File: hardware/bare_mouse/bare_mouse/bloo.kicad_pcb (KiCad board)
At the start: 2 copper layers, 103 parts, among them J1 Serial Debug Header, J10 Conn_01x06_Female, J2 SWD Header, J4 Conn_ARM_JTAG_SWD_10, J5 SWD Header, M1 M1_Conn_Alt, M2 M2_Conn_Alt, Q0 TEFT4300, Q1 TEFT4300, Q10 Q_NMOS_GSD, Q11 Q_NMOS_GSD, Q12 Q_NMOS_GSD, Q2 TEFT4300, Q3 TEFT4300, Q8 Q_NMOS_SGD, Q9 Q_NMOS_GSD, SW1 SW, SW2 SW, SW3 SW, U1 YAAJ_BluePill_SWD_Breakout, U2 L293D, U3 LM1085-5.0, U4 APE8865Y5-33-HF-3, U5 LM66100DCKR, U6 LM66100DCKR

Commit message: initial commit, starting adams pcb
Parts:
- C10: value 10uF(Tantalum) -> 10uF
- GND TP 2: renamed from TP2
- GND TP 5: renamed from TP5
- GND TP 6: renamed from TP6
- moved C1 213.4 mm to (390.6, 216.5), turned to 180 degrees
- moved C13 211.6 mm to (389.2, 225.8), turned to 180 degrees
- moved C9 210.3 mm to (392.2, 219.5), turned to 180 degrees
- moved C10 209.9 mm to (391.9, 222.5), turned to 180 degrees
- moved U3 207.7 mm to (371.1, 217.5), turned to 90 degrees
- moved BZ1 203.5 mm to (36.9, 3.28)
- moved J4 188.6 mm to (379.4, 174.7)
- moved R4 180.8 mm to (381.6, 149.9)
- moved U6 179.9 mm to (72.9, 120.1)
- moved M_MH1 179.1 mm to (342.9, 198.5)
- moved S1 178.7 mm to (349.8, 221.7)
- moved R3 175.0 mm to (375.6, 143.0)
- moved D3 170.1 mm to (384.6, 161.7), turned to 90 degrees
- moved R8 169.2 mm to (376.1, 145.9)
- moved R16 169.0 mm to (381.6, 145.9)
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- renumbered TP4 to 3V, TP3 to 5v, JP2 to JP_GND, JP3 to JP_RST, JP1 to JP_SWO, TP1 to V_EXT_TP
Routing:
- added copper zone on B.Cu, net GND
- added copper zone on F.Cu, net GND
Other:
- board outline added: 100.3 x 99 mm

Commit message: same as previous
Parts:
- C1, C10, C11, C12, C13, C14, C15, C17, C18, C19, C20, C21, C25, C3, C4, C9, L1, Q8, R11, R12, R17, R18, R19, R20, R21, R22, R23, R24, R9, U4: moved to B.Cu
- moved BZ1 364.0 mm to (327.8, 222.1), turned to 180 degrees
- moved J10 290.5 mm to (369.8, 168.2)
- moved C19 290.1 mm to (317.7, 217.9), turned to -90 degrees
- moved FB3 279.0 mm to (364.5, 187.7), turned to 180 degrees
- moved C6 277.7 mm to (359.1, 187.7), turned to 180 degrees
- moved BT_MH3 277.3 mm to (367.6, 149.2)
- moved BT_MH4 277.3 mm to (367.6, 155.2)
- moved BT_MH1 277.3 mm to (361.6, 149.2)
- moved BT_MH2 277.3 mm to (361.6, 155.2)
- moved FB4 276.5 mm to (364.5, 186.0), turned to 180 degrees
- moved C8 275.1 mm to (359.1, 186.0), turned to 180 degrees
- moved RST1 262.8 mm to (315.8, 221.1), turned to 90 degrees
- moved SW1 262.5 mm to (300.6, 221.1), turned to 90 degrees
- moved SW3 262.5 mm to (310.8, 221.1), turned to 90 degrees
- moved SW2 262.4 mm to (305.7, 221.1), turned to 90 degrees
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- renumbered SW_RST1 to RST1
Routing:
- net +3V3: track 0.00 -> 80.1 mm
- net BATT_NET: track 0.00 -> 63.5 mm, vias 0 -> 1
- net +5V_NET: track 0.00 -> 28.9 mm
- net +5V: track 0.00 -> 20.1 mm
- net Net-(S1-Pad3): track 0.00 -> 12.0 mm
- net 3V3_BYP: track 0.00 -> 7.52 mm
- net Net-(BT1-+): track 0.00 -> 6.09 mm
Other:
- board text added: "Muad' Dib Desert Mice"

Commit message: checkin changes
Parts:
- moved SK2 7.95 mm to (340.4, 131.7), turned to 180 degrees
- moved SK1 7.80 mm to (348.3, 131.7), turned to 180 degrees
- moved U1 2.68 mm to (345.2, 164.3), turned to 180 degrees

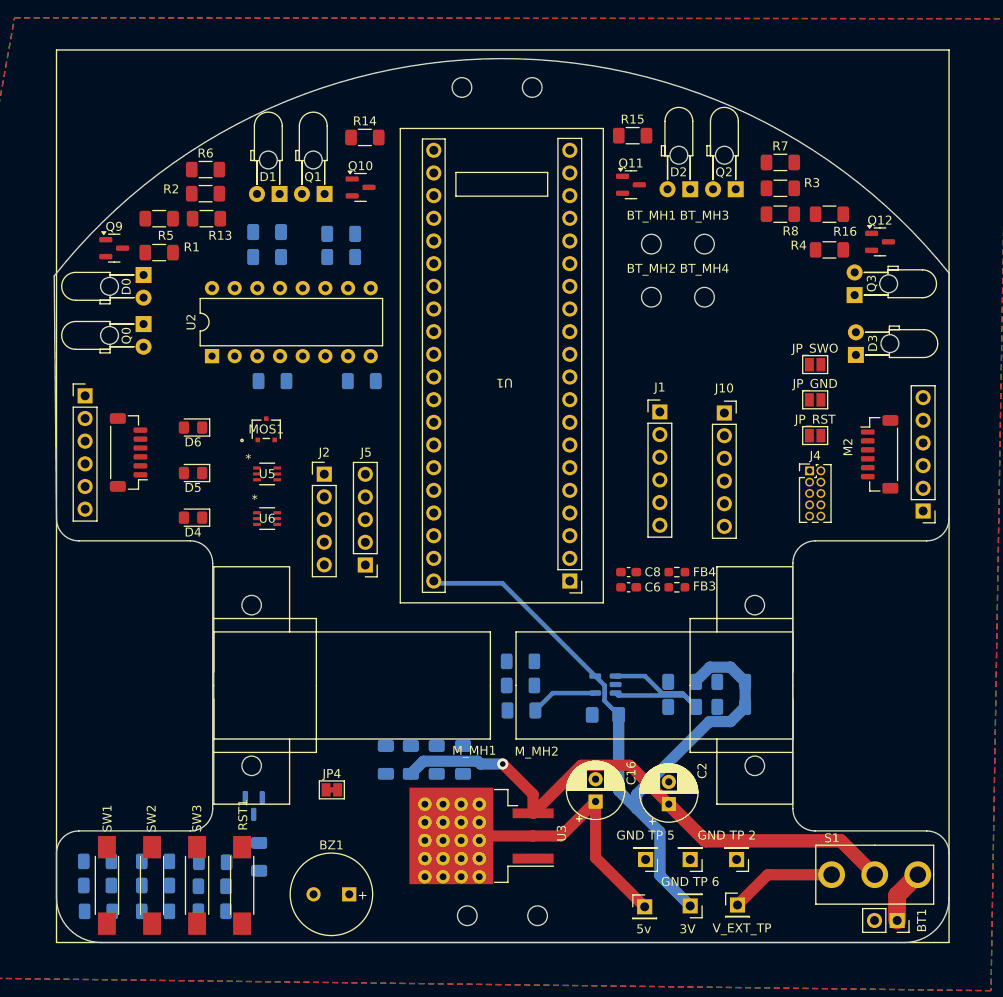
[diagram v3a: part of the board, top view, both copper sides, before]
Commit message: LED & switch wiring, mouse lost weight
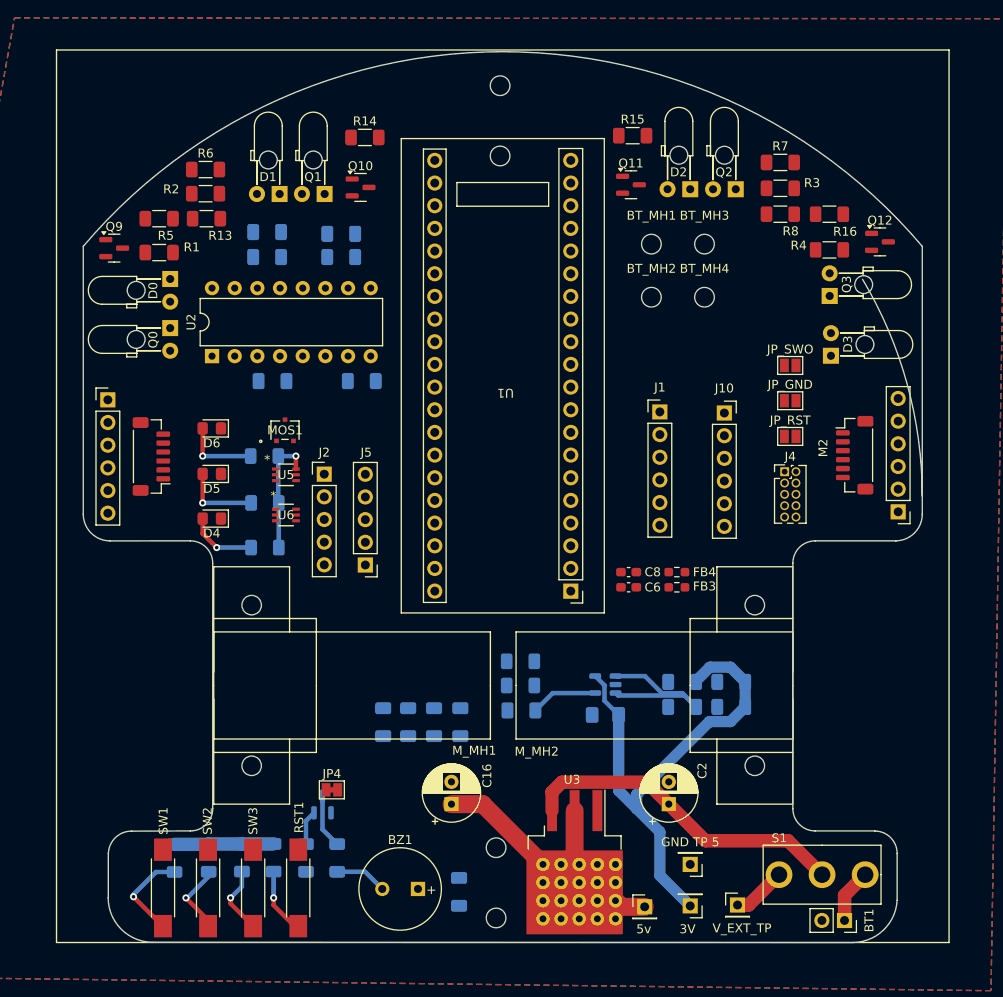
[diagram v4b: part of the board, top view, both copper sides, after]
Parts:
- removed GND TP 2: GND_TP, Connector_PinHeader_2.54mm:PinHeader_1x01_P2.54mm_Vertical
- removed GND TP 6: GND_TP, Connector_PinHeader_2.54mm:PinHeader_1x01_P2.54mm_Vertical
- moved R21 48.6 mm to (318.3, 173.0)
- moved R20 46.1 mm to (318.4, 178.2)
- moved R19 42.6 mm to (318.4, 183.2)
- moved C19 22.7 mm to (340.1, 221.8), turned to 90 degrees
- moved R18 20.4 mm to (326.4, 218.0), turned to -90 degrees
- moved R12 19.7 mm to (319.3, 218.0), turned to -90 degrees
- moved R9 17.2 mm to (315.8, 218.0), turned to -90 degrees
- moved R17 17.1 mm to (322.9, 218.0), turned to 90 degrees
- moved C16 16.2 mm to (339.2, 212.0)
- moved U3 11.3 mm to (345.0, 218.5), turned to -90 degrees
- moved R11 9.15 mm to (308.2, 218.1), turned to -90 degrees
- moved SK4 8.93 mm to (344.2, 216.9), turned to 90 degrees
- moved SK2 8.78 mm to (344.7, 139.4), turned to -90 degrees
- moved BZ1 7.72 mm to (335.5, 221.5)
- moved Q8 7.70 mm to (324.8, 212.0), turned to 90 degrees
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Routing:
- net BATT_NET: track 63.5 -> 37.1 mm, vias 1 -> 0
- net BUTTON: track 0.00 -> 10.6 mm, vias 0 -> 1
- net Net-(D5-A): track 0.00 -> 8.68 mm, vias 0 -> 1
- net Net-(D6-A): track 0.00 -> 8.47 mm, vias 0 -> 1
- net BUTTON_2: track 0.00 -> 8.26 mm, vias 0 -> 1
- net Net-(D4-A): track 0.00 -> 7.75 mm, vias 0 -> 1
- net BUTTON_3: track 0.00 -> 7.69 mm, vias 0 -> 1
- net RST: track 0.00 -> 7.50 mm, vias 0 -> 1
- net Net-(Q8-D): track 0.00 -> 6.06 mm
- net Net-(S1-Pad3): track 12.0 -> 6.06 mm
- net Net-(BZ1-+): track 0.00 -> 5.85 mm
- net BUZZER: track 0.00 -> 3.87 mm
- net +3V3: track 80.1 -> 82.5 mm, vias 0 -> 1
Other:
- board size 100.3 x 99 mm -> 94 x 99.8 mm

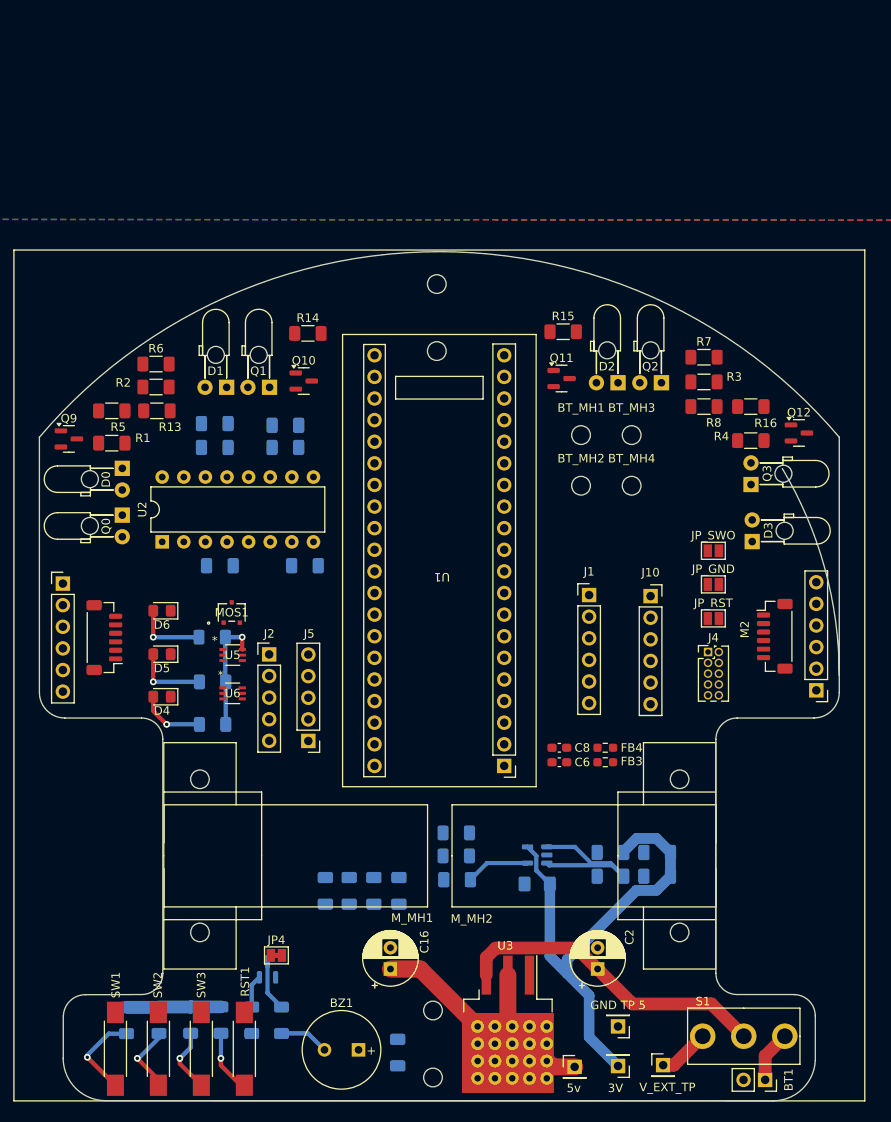
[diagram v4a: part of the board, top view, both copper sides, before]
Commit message: power ORing, SWD header, and other adam sections traced
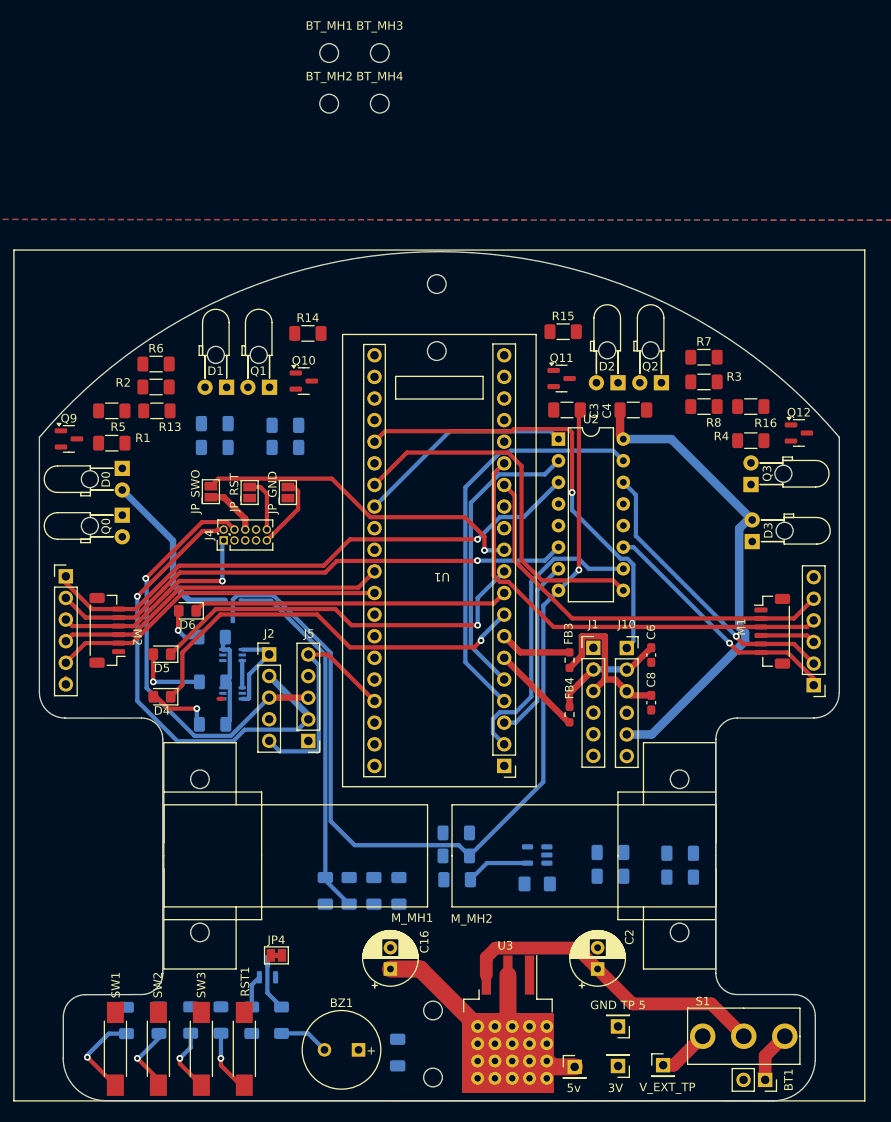
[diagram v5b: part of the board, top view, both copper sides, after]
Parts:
- C3, C4: moved to F.Cu
- MOS1, U5, U6: moved to B.Cu
- moved M1 94.8 mm to (392.2, 171.7), turned to 90 degrees
- moved M2 94.7 mm to (297.9, 172.8), turned to -90 degrees
- moved JP_SWO 59.5 mm to (318.1, 155.9), turned to 90 degrees
- moved J4 58.4 mm to (319.6, 161.6), turned to 90 degrees
- moved JP_RST 56.5 mm to (322.7, 156.0), turned to 90 degrees
- moved BT_MH3 53.8 mm to (338.0, 104.3)
- moved BT_MH4 53.8 mm to (338.0, 110.3)
- moved BT_MH1 53.8 mm to (332.1, 104.3)
- moved BT_MH2 53.8 mm to (332.1, 110.3)
- moved C4 51.9 mm to (367.8, 146.3), turned to 0 degrees
- moved JP_GND 51.2 mm to (327.2, 156.0), turned to 90 degrees
- moved U2 48.1 mm to (359.0, 149.7), turned to 0 degrees
- moved C3 35.8 mm to (360.0, 146.3), turned to 180 degrees
- moved C6 16.6 mm to (369.9, 175.1), turned to -90 degrees
- moved FB3 12.7 mm to (360.3, 175.7), turned to -90 degrees
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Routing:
- net VCC: track 0.00 -> 112.6 mm, vias 0 -> 1
- net M1_OUT_1: track 0.00 -> 66.1 mm, vias 0 -> 1
- net M1_OUT_2: track 0.00 -> 62.8 mm, vias 0 -> 1
- net +5V: track 20.1 -> 77.0 mm
- net SWDIO: track 0.00 -> 55.8 mm, vias 0 -> 1
- net M2_ENC_A: track 0.00 -> 54.1 mm
- net BLE_STATE: track 0.00 -> 53.1 mm, vias 0 -> 1
- net SWDCLK: track 0.00 -> 49.6 mm, vias 0 -> 1
- net LED_RED: track 0.00 -> 48.8 mm, vias 0 -> 1
- net M2_ENC_B: track 0.00 -> 48.3 mm
- net M2_BACK: track 0.00 -> 47.8 mm
- net LED_GREEN: track 0.00 -> 46.7 mm, vias 0 -> 1
- net M2_SPD: track 0.00 -> 44.0 mm
- net BATT_NET: track 37.1 -> 80.4 mm
- net M1_ENC_A: track 0.00 -> 39.7 mm
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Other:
- outline, holes or cut-outs redrawn

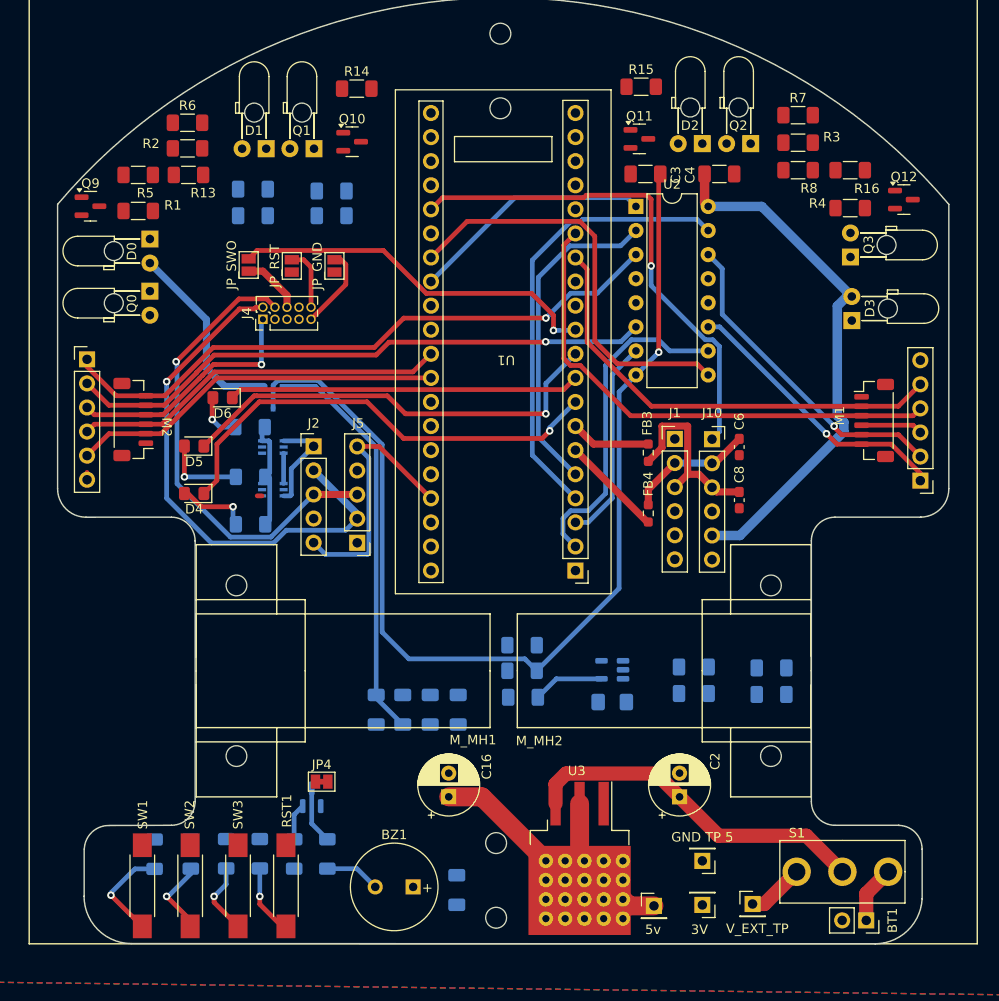
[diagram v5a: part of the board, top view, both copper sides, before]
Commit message: wiring done
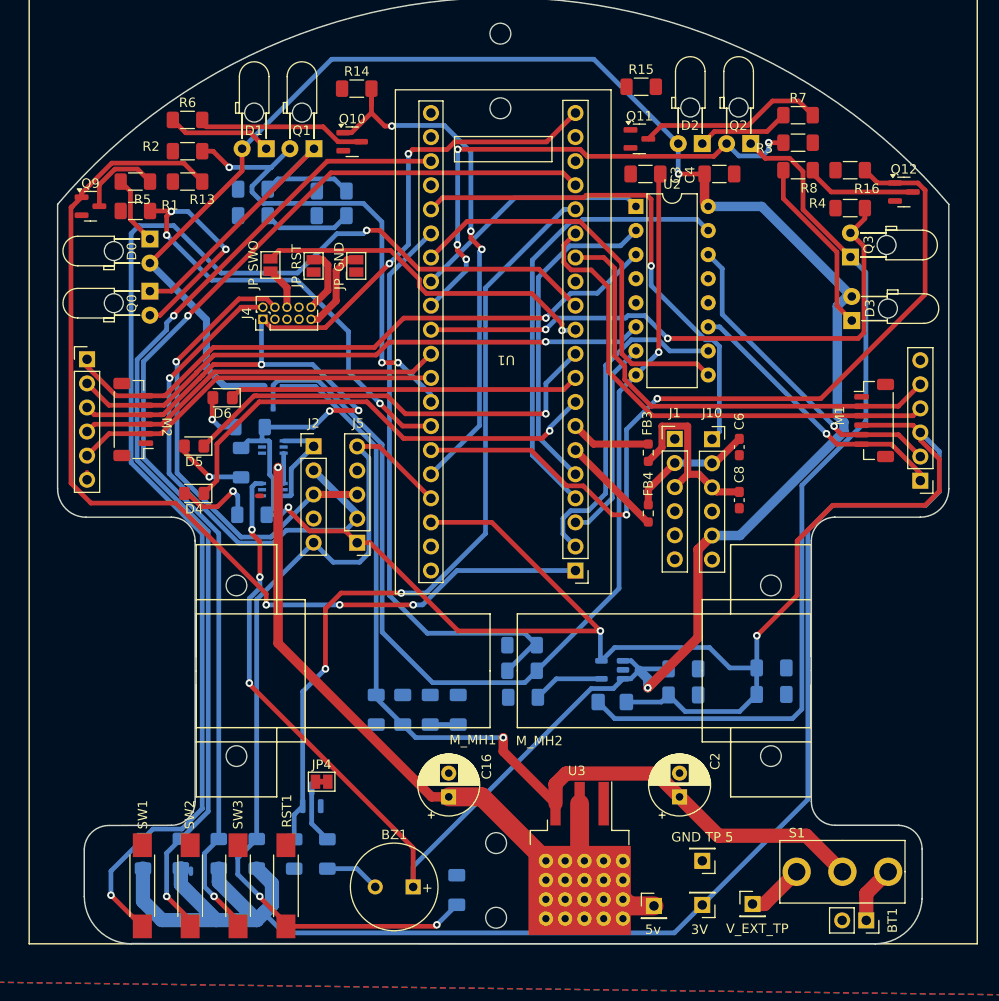
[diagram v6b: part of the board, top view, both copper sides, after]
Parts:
- moved C11 3.15 mm to (364.0, 201.2), turned to 0 degrees
- moved C17 2.82 mm to (364.0, 198.5), turned to 0 degrees
- moved JP_GND 2.30 mm to (329.5, 156.0)
- moved JP_RST 2.30 mm to (325.0, 156.0)
- moved JP_SWO 2.30 mm to (320.4, 155.9)
- moved R20 1.80 mm to (317.4, 176.8), turned to 90 degrees
- moved R11 1.23 mm to (307.0, 218.0), turned to 90 degrees
- moved R24 1.05 mm to (311.0, 218.0), turned to 90 degrees
- moved R19 1.01 mm to (318.5, 182.2)
- moved Q12 0.80 mm to (387.3, 148.2)
- moved R9 0.77 mm to (315.0, 218.0), turned to 90 degrees
- moved R5 0.76 mm to (306.2, 147.1)
- moved R13 0.71 mm to (311.7, 147.1)
- moved R12 0.32 mm to (319.0, 218.0), turned to 90 degrees
- moved R1 0.30 mm to (306.2, 150.2)
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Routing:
- net +3V3: track 44.2 -> 411.8 mm, vias 1 -> 8
- net +5V: track 77.0 -> 265.0 mm, vias 0 -> 5
- net +3.3VA: track 0.00 -> 140.4 mm
- net BUTTON: track 10.6 -> 137.8 mm, vias 1 -> 2
- net BUTTON_3: track 7.69 -> 119.4 mm, vias 1 -> 2
- net EMIT_1: track 0.00 -> 106.9 mm, vias 0 -> 3
- net BUTTON_2: track 8.26 -> 106.1 mm, vias 1 -> 2
- net EMIT_3: track 0.00 -> 88.1 mm, vias 0 -> 2
- net BUZZER: track 3.87 -> 84.7 mm, vias 0 -> 2
- net RECEIV_1: track 0.00 -> 62.0 mm, vias 0 -> 4
- net V_METER: track 0.00 -> 61.9 mm
- net RECEIV_3: track 0.00 -> 61.9 mm, vias 0 -> 2
- net RST: track 35.7 -> 93.7 mm, vias 1 -> 2
- net EMIT_2: track 0.00 -> 57.0 mm, vias 0 -> 3
- net RECEIV_4: track 0.00 -> 55.2 mm, vias 0 -> 4
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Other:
- outline, holes or cut-outs redrawn

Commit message: wiring done for real
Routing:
- net +3.3VA: track 140.4 -> 199.6 mm, vias 0 -> 4
- net RST: track 93.7 -> 141.2 mm, vias 2 -> 9
- net +5V: track 265.0 -> 262.2 mm
